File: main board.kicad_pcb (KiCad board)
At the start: 2 copper layers, 159 x 146 mm, 0 parts

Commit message: Assign footprints which close to original
Caps are assigned as close as possible
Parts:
- added C1: 0.05uF, wv98:С1, F.Cu at (50.1, 149.9)
- added C2: 0.02uF, Capacitor_THT:C_Disc_D16.0mm_W5.0mm_P10.00mm, F.Cu at (48.2, 161.4)
- added C3: 24pF, Capacitor_THT:C_Disc_D10.5mm_W5.0mm_P5.00mm, F.Cu at (77.5, 168.0)
- added C4: 0.1uF, wv98:С1, F.Cu at (50.1, 155.4)
- added C5: 0.01uF, Capacitor_THT:C_Disc_D14.5mm_W5.0mm_P10.00mm, F.Cu at (65.0, 161.4)
- added C6: 0.005uF, Capacitor_THT:C_Disc_D10.5mm_W5.0mm_P10.00mm, F.Cu at (62.2, 168.0)
- added C7: 0.01uF, Capacitor_THT:C_Disc_D14.5mm_W5.0mm_P10.00mm, F.Cu at (47.4, 168.0)
- added C8: 10uF, Capacitor_THT:CP_Radial_D8.0mm_P3.50mm, F.Cu at (147.9, 66.1)
- added CR1: 4004, Diode_THT:D_DO-41_SOD81_P5.08mm_Vertical_KathodeUp, F.Cu at (137.7, 66.1)
- added J1: #15, wv98:Hole_Din1.2mm_Dout3mm, F.Cu at (395.1, 187.9)
- added J10: #11, wv98:Hole_Din1.2mm_Dout3mm, F.Cu at (385.0, 196.0)
- added J11: #14, wv98:Hole_Din1.2mm_Dout3mm, F.Cu at (380.9, 196.0)
- added J12: #37, wv98:Hole_Din1.2mm_Dout3mm, F.Cu at (389.3, 220.3)
- added J13: #3, wv98:Hole_Din1.2mm_Dout3mm, F.Cu at (399.2, 182.8)
- added J14: #23, wv98:Hole_Din1.2mm_Dout3mm, F.Cu at (394.3, 142.8)
- added J15: #33, wv98:Hole_Din1.2mm_Dout3mm, F.Cu at (365.2, 156.9)
- added J16: #38, wv98:Hole_Din1.2mm_Dout3mm, F.Cu at (394.3, 138.8)
- added J17: #4, wv98:Hole_Din1.2mm_Dout3mm, F.Cu at (385.3, 220.3)
- added J18: #13, wv98:Hole_Din1.2mm_Dout3mm, F.Cu at (389.3, 216.2)
- added J19: #9, wv98:Hole_Din1.2mm_Dout3mm, F.Cu at (383.0, 192.0)
- added J2: Red-Blk, wv98:Hole_Din1.2mm_Dout3mm, F.Cu at (394.6, 150.9)
- added J20: #18, wv98:Hole_Din1.2mm_Dout3mm, F.Cu at (387.0, 187.9)
- added J21: #22, wv98:Hole_Din1.2mm_Dout3mm, F.Cu at (391.1, 183.9)
- added J22: #21, wv98:Hole_Din1.2mm_Dout3mm, F.Cu at (395.1, 179.8)
- added J23: #25, wv98:Hole_Din1.2mm_Dout3mm, F.Cu at (399.2, 178.7)
- added J24: #8, wv98:Hole_Din1.2mm_Dout3mm, F.Cu at (391.1, 179.8)
- added J25: #16, wv98:Hole_Din1.2mm_Dout3mm, F.Cu at (383.0, 187.9)
- added J26: #12, wv98:Hole_Din1.2mm_Dout3mm, F.Cu at (387.0, 179.8)
- added J27: #35, wv98:Hole_Din1.2mm_Dout3mm, F.Cu at (391.1, 192.0)
- added J28: #7, wv98:Hole_Din1.2mm_Dout3mm, F.Cu at (302.9, 187.0)
- added J29: #19, wv98:Hole_Din1.2mm_Dout3mm, F.Cu at (335.7, 145.5)
- added J3: #2, wv98:Hole_Din1.2mm_Dout3mm, F.Cu at (399.2, 186.8)
- added J30: #26, wv98:Hole_Din1.2mm_Dout3mm, F.Cu at (339.8, 145.5)
- added J31: #5, wv98:Hole_Din1.2mm_Dout3mm, F.Cu at (307.0, 187.0)
- added J32: #28, wv98:Hole_Din1.2mm_Dout3mm, F.Cu at (373.1, 215.6)
- added J33: #32, wv98:Hole_Din1.2mm_Dout3mm, F.Cu at (377.2, 215.6)
- added J34: #39, wv98:Hole_Din1.2mm_Dout3mm, F.Cu at (373.1, 219.7)
- added J35: #27, wv98:Hole_Din1.2mm_Dout3mm, F.Cu at (354.9, 140.3)
- added J36: #40, wv98:Hole_Din1.2mm_Dout3mm, F.Cu at (383.0, 179.8)
- added J37: #17, wv98:Hole_Din1.2mm_Dout3mm, F.Cu at (397.4, 217.6)
- added J38: #20, wv98:Hole_Din1.2mm_Dout3mm, F.Cu at (383.0, 183.9)
- added J39: #24, wv98:Hole_Din1.2mm_Dout3mm, F.Cu at (377.2, 219.7)
- added J4: Blk, wv98:Hole_Din1.2mm_Dout3mm, F.Cu at (394.6, 146.9)
- added J40: #29, wv98:Hole_Din1.2mm_Dout3mm, F.Cu at (381.2, 215.6)
- added J41: #30, wv98:Hole_Din1.2mm_Dout3mm, F.Cu at (385.3, 212.2)
- added J42: #31, wv98:Hole_Din1.2mm_Dout3mm, F.Cu at (394.3, 130.7)
- added J43: #34, wv98:Hole_Din1.2mm_Dout3mm, F.Cu at (361.1, 156.9)
- added J44: #36, wv98:Hole_Din1.2mm_Dout3mm, F.Cu at (394.3, 134.7)
- added J45: #Brn, wv98:Hole_Din1.2mm_Dout3mm, F.Cu at (389.3, 212.2)
- added J46: #Blu, wv98:Hole_Din1.2mm_Dout3mm, F.Cu at (385.3, 216.2)
- added J47: #L2, wv98:Hole_Din1.2mm_Dout3mm, F.Cu at (381.2, 219.7)
- added J48: #L1, wv98:Hole_Din1.2mm_Dout3mm, F.Cu at (387.0, 183.9)
- added J5: #1, wv98:Hole_Din1.2mm_Dout3mm, F.Cu at (403.3, 178.7)
- added J6: #6, wv98:Hole_Din1.2mm_Dout3mm, F.Cu at (395.1, 183.9)
- added J7: #10, wv98:Hole_Din1.2mm_Dout3mm, F.Cu at (115.6, 181.1)
- added J8: Red-Yel, wv98:Hole_Din1.2mm_Dout3mm, F.Cu at (387.0, 192.0)
- added J9: Red-Grn, wv98:Hole_Din1.2mm_Dout3mm, F.Cu at (393.4, 217.6)
- added R1: 150k, wv98:R1-like, F.Cu at (142.6, 163.1)
- added R10: 91M, Resistor_THT:R_Axial_DIN0411_L9.9mm_D3.6mm_P15.24mm_Horizontal, F.Cu at (222.6, 79.3)
- added R11: 16M, wv98:R2, F.Cu at (132.4, 117.7)
- added R12: 7M, wv98:R12, F.Cu at (165.4, 180.7)
- added R2: 324k, wv98:R2, F.Cu at (110.5, 132.9)
- added R23: 10k, Resistor_THT:R_Axial_DIN0411_L9.9mm_D3.6mm_P20.32mm_Horizontal, F.Cu at (186.2, 163.1)
- added R24: 10k, Resistor_THT:R_Axial_DIN0411_L9.9mm_D3.6mm_P20.32mm_Horizontal, F.Cu at (187.3, 155.5)
- added R25: 3.3M, Resistor_THT:R_Axial_DIN0411_L9.9mm_D3.6mm_P15.24mm_Horizontal, F.Cu at (218.2, 163.1)
- added R26: 6.8M, Resistor_THT:R_Axial_DIN0411_L9.9mm_D3.6mm_P15.24mm_Horizontal, F.Cu at (214.7, 127.6)
- added R27: 330, Resistor_THT:R_Axial_DIN0411_L9.9mm_D3.6mm_P20.32mm_Horizontal, F.Cu at (191.3, 169.7)
- added R28: 330, Resistor_THT:R_Axial_DIN0411_L9.9mm_D3.6mm_P20.32mm_Horizontal, F.Cu at (204.0, 155.5)
- added R3: 900k, wv98:R3, F.Cu at (101.7, 104.5)
- added R30: 27k, Resistor_THT:R_Axial_DIN0411_L9.9mm_D3.6mm_P15.24mm_Horizontal, F.Cu at (175.3, 144.1)
- added R31: 1M, Resistor_THT:R_Axial_DIN0411_L9.9mm_D3.6mm_P15.24mm_Horizontal, F.Cu at (148.9, 142.1)
- added R32: 47k, Resistor_THT:R_Axial_DIN0411_L9.9mm_D3.6mm_P15.24mm_Horizontal, F.Cu at (215.2, 79.8)
- added R34: 180k, Resistor_THT:R_Axial_DIN0411_L9.9mm_D3.6mm_P15.24mm_Horizontal, F.Cu at (124.0, 80.1)
- added R39: 1k, Resistor_THT:R_Axial_DIN0411_L9.9mm_D3.6mm_P15.24mm_Horizontal, F.Cu at (122.2, 181.2)
- added R4: 9.75, wv98:R2, F.Cu at (138.5, 179.3)
- added R5: 100, wv98:R1-like, F.Cu at (161.3, 187.8)
- added R6: 1k, wv98:R1-like, F.Cu at (154.0, 187.8)
- added R7: 10k, wv98:R1-like, F.Cu at (146.4, 187.8)
- added R8: 2.12M, wv98:R1-like, F.Cu at (170.5, 189.8)
- added R9: 8.49M, wv98:R1-like, F.Cu at (168.7, 147.4)
- added RV19: 10k, Potentiometer_THT:Potentiometer_Piher_PT-15-H01_Horizontal, F.Cu at (246.2, 104.5)
- added RV20: 10k, Potentiometer_THT:Potentiometer_Piher_PT-15-H01_Horizontal, F.Cu at (246.2, 123.8)
- added RV21: 10k, Potentiometer_THT:Potentiometer_Piher_PT-15-H01_Horizontal, F.Cu at (246.2, 142.1)
- added RV33: 10k, Potentiometer_THT:Potentiometer_Piher_PT-15-H01_Horizontal, F.Cu at (246.2, 160.9)
- added RV35: 10k, wv98:R35, F.Cu at (116.4, 114.4)
- added U1: 6AL5, wv98:6AL5, F.Cu at (126.3, 144.8)
- added U2: ECC83, wv98:12AU7A original socket, F.Cu at (222.3, 144.8)
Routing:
- net Net-(J7-Pad1): track 0.00 -> 6.10 mm
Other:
- net class Default: clearance 0.2 -> 0.5; trace_width 0.25 -> 1.5; via_dia 0.8 -> 1; via_drill 0.4 -> 0.8
- rule trace_clearance: 0.2 -> 0.5
- rule trace_min: 0.2 -> 1.5
- rule via_min_drill: 0.3 -> 0.8
- rule via_min_size: 0.4 -> 1

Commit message: Align all holes as close to original as possible
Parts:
- removed J34: #39, wv98:Hole_Din1.2mm_Dout3mm
- added Je: #39, wv98:Hole_Din1.2mm_Dout3mm, F.Cu at (106.4, 104.7)
- U2: footprint wv98:12AU7A original socket -> wv98:12AU7A
- moved J46 301.9 mm to (118.3, 75.3)
- moved J45 297.4 mm to (125.3, 75.3)
- moved J37 296.9 mm to (104.3, 170.3)
- moved J47 291.3 mm to (132.9, 67.3)
- moved J9 288.2 mm to (142.8, 75.3)
- moved J38 282.3 mm to (100.8, 176.3)
- moved J40 281.8 mm to (100.8, 188.3)
- moved J36 280.4 mm to (107.8, 126.1)
- moved J39 278.9 mm to (100.8, 182.3)
- moved J6 276.3 mm to (119.8, 160.5)
- moved J48 274.9 mm to (138.1, 67.3)
- moved J3 271.2 mm to (138.8, 110.8)
- moved J22 268.3 mm to (126.8, 176.3)
- moved J23 265.7 mm to (133.6, 183.7)
- moved J8 264.8 mm to (149.3, 75.3)
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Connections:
- RV35 pad 3: (no net) -> Net-(J36-Pad1)
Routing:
- net Net-(C8-Pad1): track 0.00 -> 102.8 mm
- net Net-(J4-Pad1): track 0.00 -> 50.0 mm
- net R34: track 0.00 -> 25.0 mm
- net Net-(C8-Pad2): track 0.00 -> 19.1 mm
- net Net-(J31-Pad1): track 0.00 -> 9.11 mm
- net Net-(CR1-Pad2): track 0.00 -> 9.02 mm
- net Net-(J34-Pad1): track 0.00 -> 7.92 mm
- net Net-(J36-Pad1): track 0.00 -> 7.17 mm
- net Net-(J28-Pad1): track 0.00 -> 6.40 mm
- net Net-(J7-Pad1): track 6.10 -> 0.00 mm
- net Net-(J47-Pad1): track 0.00 -> 5.66 mm
- net Net-(J29-Pad1): track 0.00 -> 5.20 mm
- net Net-(J19-Pad1): track 0.00 -> 4.66 mm
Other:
- outline, holes or cut-outs redrawn

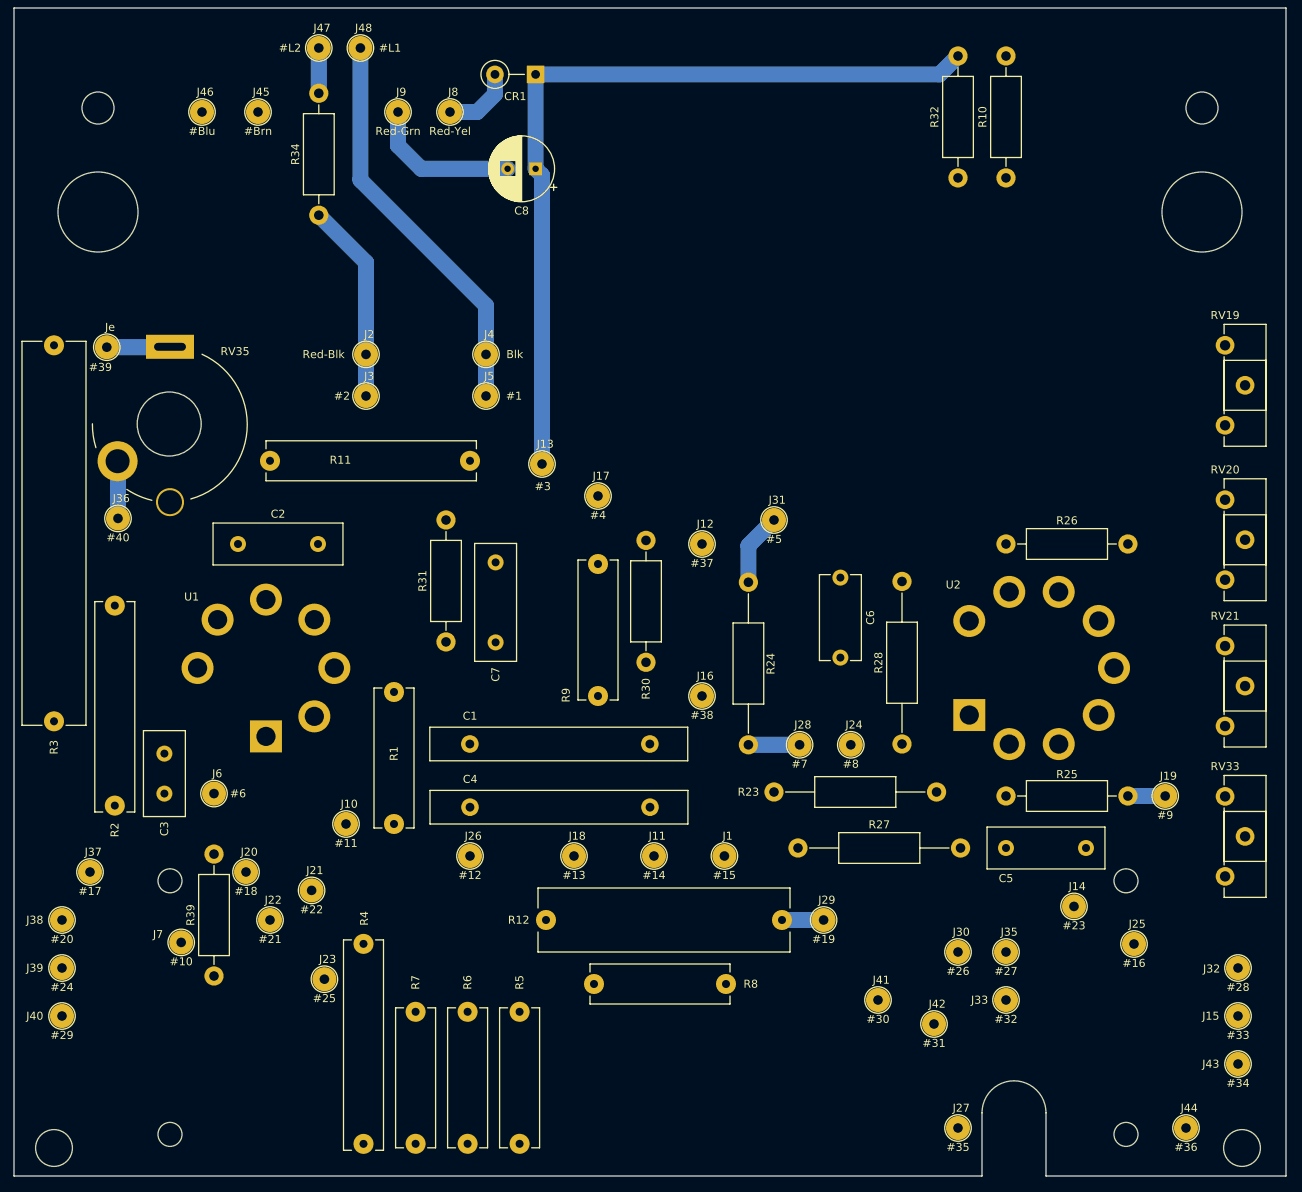
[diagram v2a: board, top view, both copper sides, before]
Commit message: Add big 4 node resistor and layout close to original
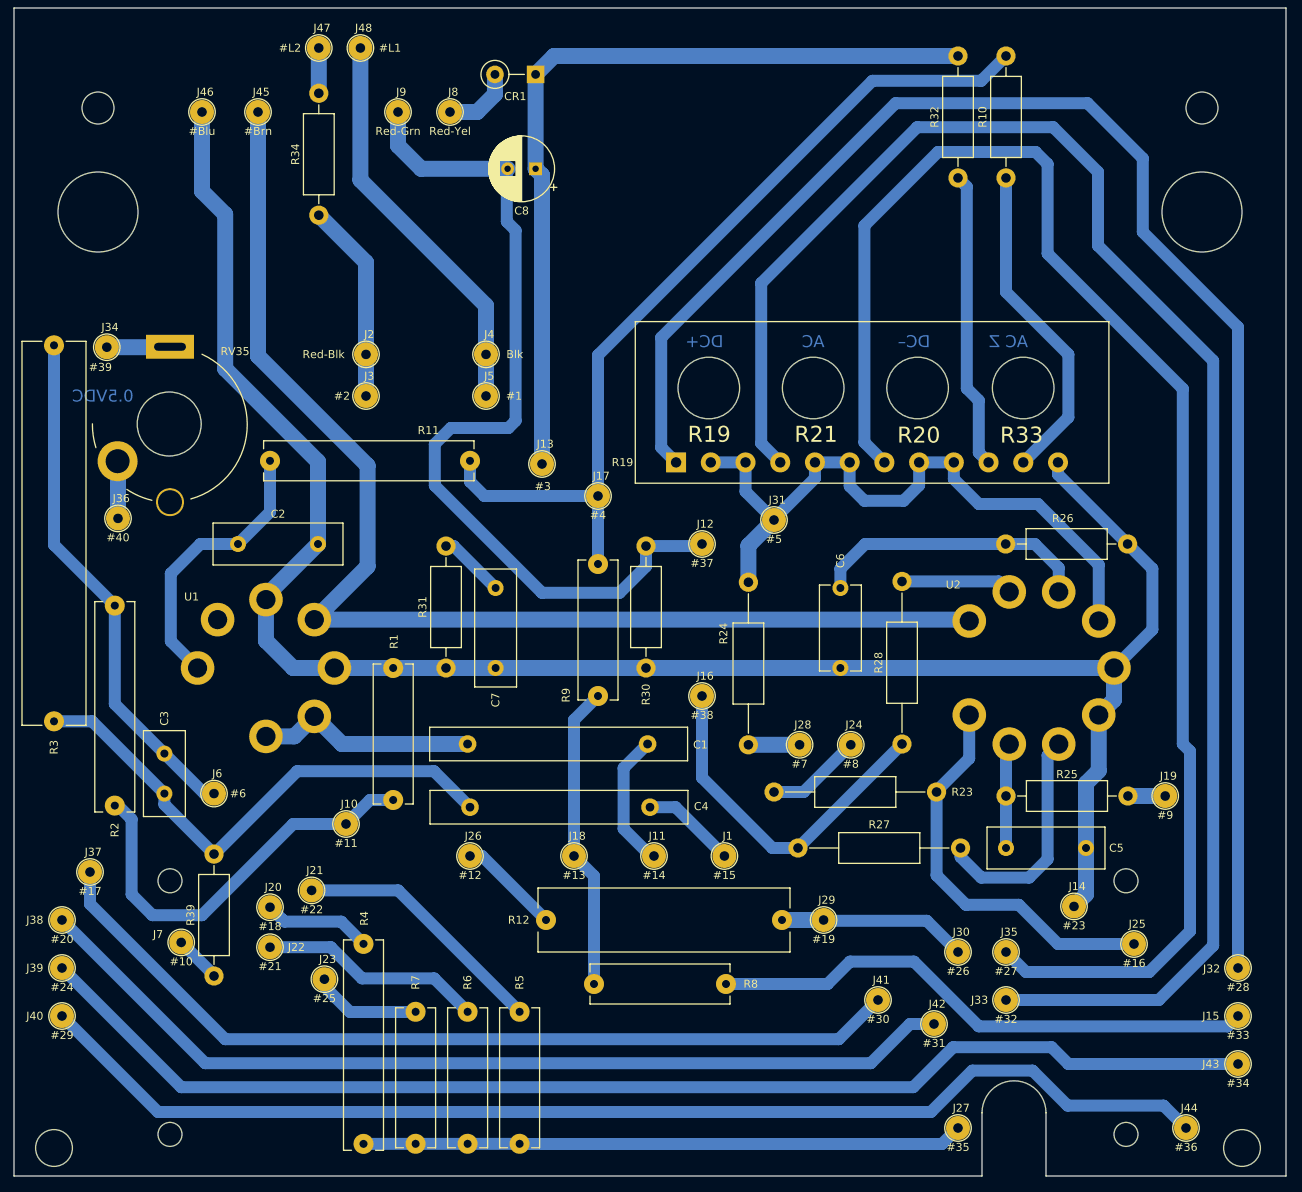
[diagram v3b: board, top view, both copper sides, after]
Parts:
- removed RV19, RV20, RV21, RV33: 10k, Potentiometer_THT:Potentiometer_Piher_PT-15-H01_Horizontal
- added ?: , , F.Cu at (66.9, -1.00)
- added ?: , , F.Cu at (64.3, -6.20)
- added ?: , , F.Cu at (65.0, -12.1)
- added ?: , , F.Cu at (172.8, 62.1)
- added R19: R-4, wv98:R-4-in-row, F.Cu at (177.6, 119.1)
- moved R11 25.0 mm to (151.8, 118.9), turned to 180 degrees
- moved C1 22.2 mm to (174.0, 154.3), turned to 180 degrees
- moved R23 20.3 mm to (210.1, 160.3), turned to 180 degrees
- moved R26 15.2 mm to (234.0, 129.3), turned to 180 degrees
- moved C5 10.0 mm to (228.8, 167.3), turned to 180 degrees
- moved J20 5.33 mm to (126.8, 174.7)
- moved C3 5.00 mm to (113.6, 155.5), turned to 270 degrees
- moved J22 3.40 mm to (126.8, 179.7)
- moved R31 3.26 mm to (148.8, 144.8)
- moved C7 3.20 mm to (155.0, 134.8)
- moved R1 3.00 mm to (142.2, 161.3)
- moved C6 1.30 mm to (198.1, 134.8)
- moved R30 0.71 mm to (173.8, 144.8)
- renumbered Je to J34
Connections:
- RV35 pad 3: Net-(J36-Pad1) -> (no net)
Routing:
- net GND: track 0.00 -> 246.7 mm
- net Net-(J33-Pad1): track 0.00 -> 207.3 mm
- net Net-(J32-Pad1): track 0.00 -> 197.7 mm
- net Net-(J35-Pad1): track 0.00 -> 187.4 mm
- net Net-(J39-Pad1): track 0.00 -> 156.1 mm
- net Net-(J45-Pad1): track 0.00 -> 153.8 mm
- net Net-(J40-Pad1): track 0.00 -> 150.6 mm
- net Net-(J38-Pad1): track 0.00 -> 118.4 mm
- net Net-(J17-Pad1): track 0.00 -> 111.9 mm
- net Net-(J37-Pad1): track 0.00 -> 111.5 mm
- net Net-(C8-Pad2): track 19.1 -> 110.6 mm
- net Net-(J31-Pad1): track 9.11 -> 87.8 mm
- net Net-(J27-Pad1): track 0.00 -> 75.2 mm
- net Net-(J15-Pad1): track 0.00 -> 69.1 mm
- net Net-(C3-Pad2): track 0.00 -> 65.8 mm
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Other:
- outline, holes or cut-outs redrawn
- board text added: "0.5VDC"
- board text added: "AC"
- board text added: "AC Z"
- board text added: "DC+"
- board text added: "DC–"
- board text added: "Right R hole"
